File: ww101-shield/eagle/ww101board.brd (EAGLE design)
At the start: 59.1 x 64.6 mm, 58 parts

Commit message: Updated Test Program
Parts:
- moved MB0 9.60 mm to (24.7, 44.7)
- moved MB1 9.60 mm to (24.7, 54.3)
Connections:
- net MB0: now also JP1.2, R10.2, U$7.29; no longer JP1.1, R9.2, U$7.28
- net MB1: now also JP1.1, R9.2, U$7.28; no longer JP1.2, R10.2, U$7.29
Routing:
- net MB0: track 78.6 -> 76.2 mm, vias 5 -> 7
- net MB1: track 76.3 -> 78.6 mm, vias 7 -> 5

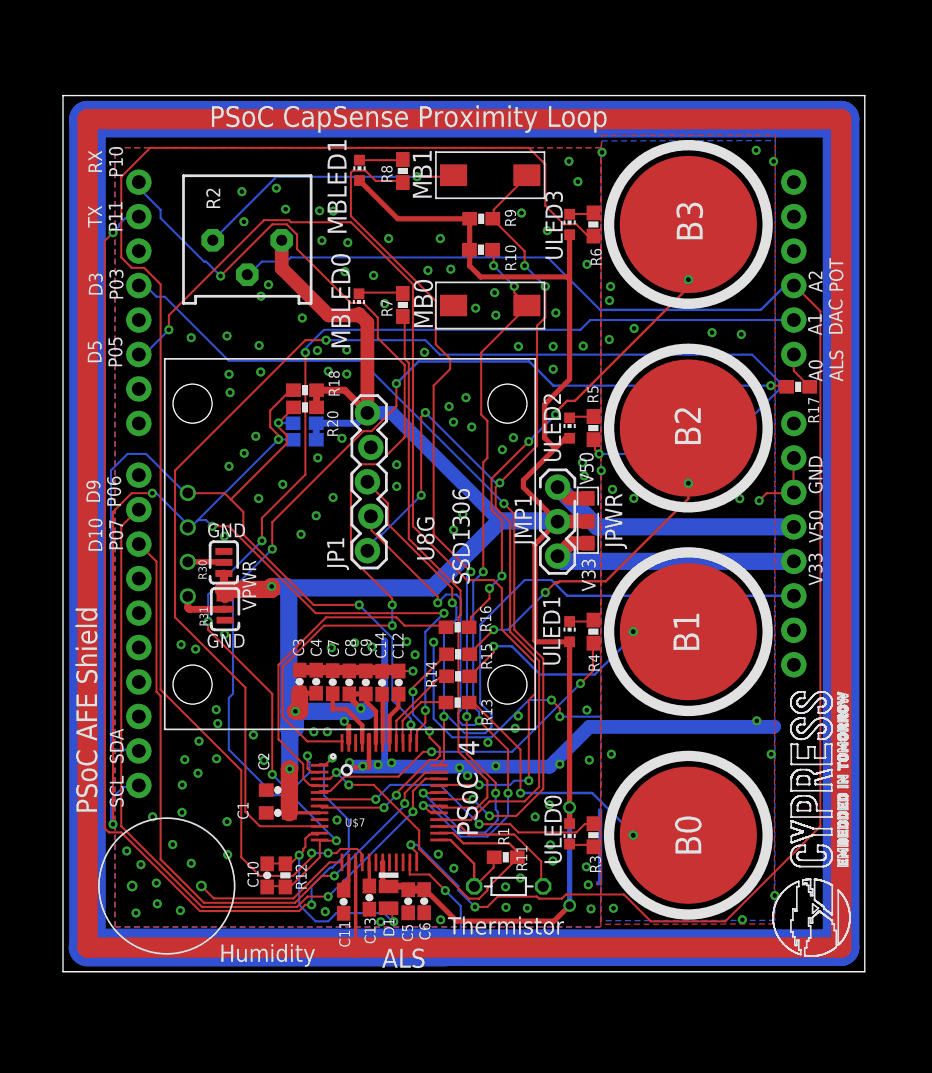
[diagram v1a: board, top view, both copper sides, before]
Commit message: Updated silkscreen
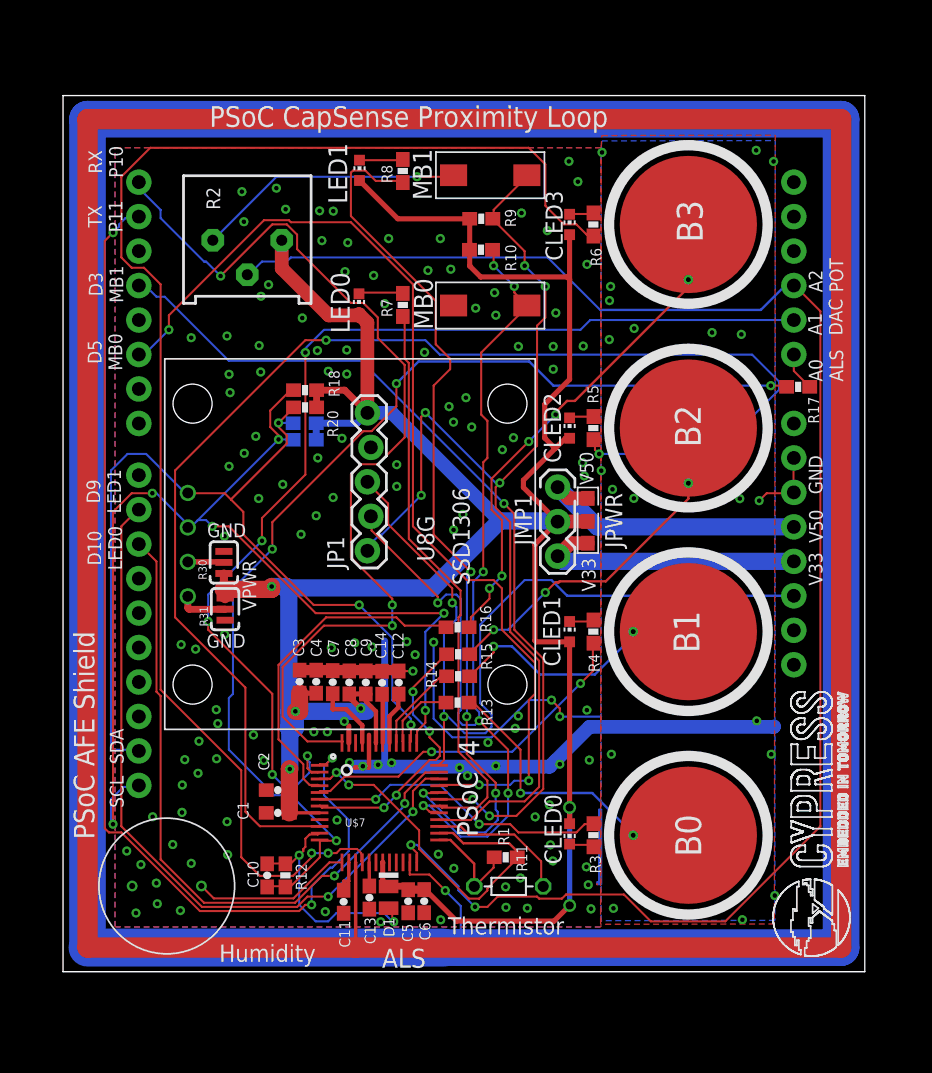
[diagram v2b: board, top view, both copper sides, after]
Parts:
- renumbered MBLED0 to LED0, MBLED1 to LED1, ULED0 to CLED0, ULED1 to CLED1, ULED2 to CLED2, ULED3 to CLED3
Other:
- board text added: "D10 LED0"
- board text added: "D3 MB1"
- board text added: "D5 MB0"
- board text added: "D9 LED1"
- board text added: "PSoC Function P24 Humidity Ref Cap P25 Proximity P26 CapLED 3 P27 SAR Bypass P30 Unused P31 Unused P32 Unused P33 Prox Shield P34 Pot ARD-A3"
- board text added: "PSoC Function P35 Therm - MID P36 Therm Ref (1.2V) P37 Therm Low (GND) P40 SCL P41 SDA P50 CapSense B0 P51 CapSense B1 P52 CMOD P53 CTANK"
- board text removed: "D10 P07"
- board text removed: "D3 P03"
- board text removed: "D5 P05"
- board text removed: "D9 P06"
- board text removed: "PSoC Function P23 Humidity Sensor P24 Humidity Ref Cap P25 Proximity P26 CapLED 3 P27 SAR Bypass P33 Prox Shield P34 Pot ARD-A3 P35 Therm - MID P36 Therm Ref (1.2V) P37 Therm Low (GND)"
- board text removed: "PSoC Function P40 SCL P41 SDA P50 CapSense B0 P51 CapSense B1 P52 CMOD P53 CTANK"

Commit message: Right before autoroute
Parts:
- added LED2: red, adafruit:CHIP-LED0603
- added R22: 10K, PatternAgents-ProtoPads:0603-RES
- added R23: 560, PatternAgents-ProtoPads:0603-RES
- moved R11 0.56 mm to (29.5, 3.24)
- moved C3 0.15 mm to (14.2, 17.8)
- moved C6 0.15 mm to (23.6, 1.52)
- moved C13 0.14 mm to (19.4, 1.78)
- moved D1 0.13 mm to (20.9, 3.10)
- moved C4 0.12 mm to (15.5, 17.8)
- moved C5 0.11 mm to (22.4, 1.52)
- moved C7 0.09 mm to (16.7, 17.8)
- moved C8 0.06 mm to (18.0, 17.8)
- renumbered MB0 to MB2
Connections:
- net MBLED1 renamed LED1
- removed net D10: U$1.D10, U$7.35
- removed net D3: U$1.D3, U$7.31
- removed net D9: U$1.D9, U$7.34
- removed net MB0: JP1.2, MB2.P$2, R10.2, U$7.29
- removed net MBLED0: R7.1, U$7.30
- new net D11: U$1.D11, U$7.35
- new net D12: U$1.D12, U$7.30
- new net D13: U$1.D13, U$7.21
- new net D4: U$1.D4, U$7.31
- new net FUTUREARD: U$1.D2, U$7.22
- new net LED2: R7.1, U$7.34
- new net MB2: JP1.1, MB2.P$2, R10.2, U$7.28
- new net N$3: LED2.C, R23.2
- new net PROXLED: R23.1, U$7.20
- net MB1: now also JP1.2, U$7.29; no longer JP1.1, U$7.28
- net VPWR: now also LED2.A, R22.1
- net XRES: now also R22.2
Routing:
- net CSHIELD: track 241.8 -> 6.92 mm, vias 1 -> 2
- net GND: track 129.0 -> 3.47 mm, vias 151 -> 2
- net POT: track 122.0 -> 0.00 mm, vias 2 -> 0
- net CBLED3: track 105.8 -> 0.00 mm, vias 2 -> 0
- net CBLED2: track 100.0 -> 0.00 mm, vias 2 -> 0
- net SCL: track 81.4 -> 0.00 mm, vias 6 -> 0
- net VDAC: track 80.3 -> 0.00 mm, vias 5 -> 0
- net UARTRX: track 78.8 -> 0.00 mm, vias 3 -> 0
- net MB1: track 78.6 -> 0.00 mm, vias 5 -> 0
- net MB0: track 76.2 -> 0.00 mm, vias 7 -> 0
- net D5: track 75.3 -> 0.00 mm, vias 3 -> 0
- net TIA_OUT: track 80.8 -> 6.73 mm, vias 4 -> 0
- net UARTTX: track 71.6 -> 0.00 mm, vias 3 -> 0
- net SDA: track 69.1 -> 0.00 mm, vias 3 -> 0
- net LED1: track 66.2 -> 0.00 mm, vias 4 -> 0
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- added copper zone on layer 16, net CSHIELD
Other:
- board size 59.1 x 64.6 mm -> 64.5 x 73.1 mm

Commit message: V2.0 of board
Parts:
- removed LED0: red, adafruit:CHIP-LED0603
- added PROX: red, adafruit:CHIP-LED0603
- added R24: 0R, PatternAgents-ProtoPads:0603-RES
- moved LED2 56.0 mm to (18.8, 55.5), turned to 0 degrees
- moved LED1 9.85 mm to (18.7, 45.6)
- moved MB1 9.60 mm to (24.7, 44.7)
- moved MB2 9.60 mm to (24.7, 54.3)
- moved R12 2.27 mm to (11.6, 5.03)
- moved C10 2.27 mm to (10.3, 5.03)
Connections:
- new net CMESH: R24.1
- net CSHIELD: now also R24.2
- net LED1: now also R7.1, U$7.34; no longer R8.1, U$7.32
- net LED2: now also R8.1, U$7.32; no longer R7.1, U$7.34
- net MB1: now also JP1.1, R10.2, U$7.28; no longer JP1.2, R9.2, U$7.29
- net MB2: now also JP1.2, R9.2, U$7.29; no longer JP1.1, R10.2, U$7.28
- net N$12: now also LED1.C; no longer LED0.C
- net N$13: now also LED2.C; no longer LED1.C
- net N$3: now also PROX.C; no longer LED2.C
- net VPWR: now also PROX.A; no longer LED0.A
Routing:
- net TIA_OUT: track 6.73 -> 141.8 mm
- net POT: track 0.00 -> 135.0 mm, vias 0 -> 2
- net MB1: track 0.00 -> 132.9 mm, vias 0 -> 4
- net D5: track 0.00 -> 128.6 mm, vias 0 -> 3
- net LED2: track 0.00 -> 106.3 mm, vias 0 -> 6
- net VDAC: track 0.00 -> 105.2 mm, vias 0 -> 2
- net CBLED3: track 0.00 -> 89.2 mm, vias 0 -> 2
- net CBLED2: track 0.00 -> 81.5 mm, vias 0 -> 2
- net FUTUREARD: track 0.00 -> 79.3 mm, vias 0 -> 3
- net GND: track 3.47 -> 81.6 mm, vias 2 -> 94
- net XRES: track 0.00 -> 74.5 mm, vias 0 -> 2
- net SCL: track 0.00 -> 68.9 mm, vias 0 -> 2
- net D4: track 0.00 -> 68.8 mm, vias 0 -> 1
- net D11: track 0.00 -> 64.8 mm, vias 0 -> 3
- net SDA: track 0.00 -> 64.7 mm, vias 0 -> 2
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- added copper zone on layer 16, net CMESH
- removed copper zone on layer 16, net CSHIELD
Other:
- board text added: "A0:ALS"
- board text added: "A1:DAC"
- board text added: "A2:POT"
- board text added: "D2"
- board text added: "INT:D13"
- board text added: "LED1:D5"
- board text added: "LED2:D11"
- board text added: "MB1:D4"
- board text added: "MB2"
- board text added: "MB2:D12"
- board text added: "PSoC AFE Shield V2.0"
- board text added: "PSoC Function P00 MB2/SDAT P01 MB1/SCLK P02 D12 P03 D4 P04 LED2 P05 D5 P06 LED1 P07 D11 P10 ARD-RX P11 ARD-TX"
- board text added: "PSoC Function P12 VDAC ARD-A1 P13 Therm Ref P14 CapSense B3 P15 CapLED 1 P16 CapLED 0 P17 CapSense B2 P20 CapLED 2 P21 TIAIN P22 TIAOUT ARD-A0 P23 Humidity"
- board text added: "PSoC Function P24 Humidity Ref Cap P25 Proximity P26 CapLED 3 P27 SAR Bypass P30 PROX LED P31 D13 P32 D2 P33 Prox Shield P34 Pot ARD-A3"
- board text added: "PSoC Function P35 Therm Mid P36 Therm Ref P37 Therm Low (GND) P40 SCL P41 SDA P50 CapSense B0 P51 CapSense B1 P52 CMOD P53 CTANK"
- board text added: "RX:D0"
- board text added: "TX:D1"
- board text added: "Therm"
- board text removed: "A0 ALS"
- board text removed: "A1 DAC"
- board text removed: "A2 POT"
- board text removed: "D10 LED0"
- board text removed: "D3 MB1"
- board text removed: "D5 MB0"
- board text removed: "D9 LED1"
- board text removed: "MB0"
- board text removed: "PSoC AFE Shield"
- board text removed: "PSoC Function P00 MB0 P01 MB1 P02 MBLED0 P03 ARD-D3 P04 MBLED1 P05 ARD-D5 P06 ARD-D9 P07 ARD-D10 P10 ARD-RX P11 ARD-TX"
- board text removed: "PSoC Function P12 VDAC ARD-A1 P13 THERM-REF P14 CapSense B3 P15 CapLED 1 P16 CapLED 0 P17 CapB2 P20 CapLED 2 P21 TIA-IN P22 TIAOUT ARD-A0 P23 Humidity"
- board text removed: "PSoC Function P24 Humidity Ref Cap P25 Proximity P26 CapLED 3 P27 SAR Bypass P30 Unused P31 Unused P32 Unused P33 Prox Shield P34 Pot ARD-A3"
- board text removed: "PSoC Function P35 Therm - MID P36 Therm Ref (1.2V) P37 Therm Low (GND) P40 SCL P41 SDA P50 CapSense B0 P51 CapSense B1 P52 CMOD P53 CTANK"
- board text removed: "RX P10"
- board text removed: "TX P11"
- board text removed: "Thermistor"
